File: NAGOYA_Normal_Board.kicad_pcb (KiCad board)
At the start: 2 copper layers, 60 x 71 mm, 104 parts, among them CN1 XT30-M, CN13 value, CN14 RefereeSystem, CN15 micro_B, CN2 XT30-M, CN3 XT30-F, CN4 XT30-F, CN5 XT30-F, CN6 XT30-F, J1 debug, J10 CAN3, J13 CAN3, J14 CAN3, J5 CAN3, J6 CAN3, J7 CAN3, J8 CAN3, J9 CAN3, Q2 DDTC114EUA-7-F, Q4 DDTC114EUA-7-F, Q5 DDTC114EUA-7-F, Q6 DDTC114EUA-7-F, SW1 SW_DIP_x04, U1 Teensy4.1, U2 TCAN1042HVDR, U3 TCAN1042HVDR, U4 TCAN1042HVDR, U5 FT234XD, U6 TLP172AM, U7 BNO055, U8 ADuM121N, U9 LXES11DAA2-137, Y2 32.768 k

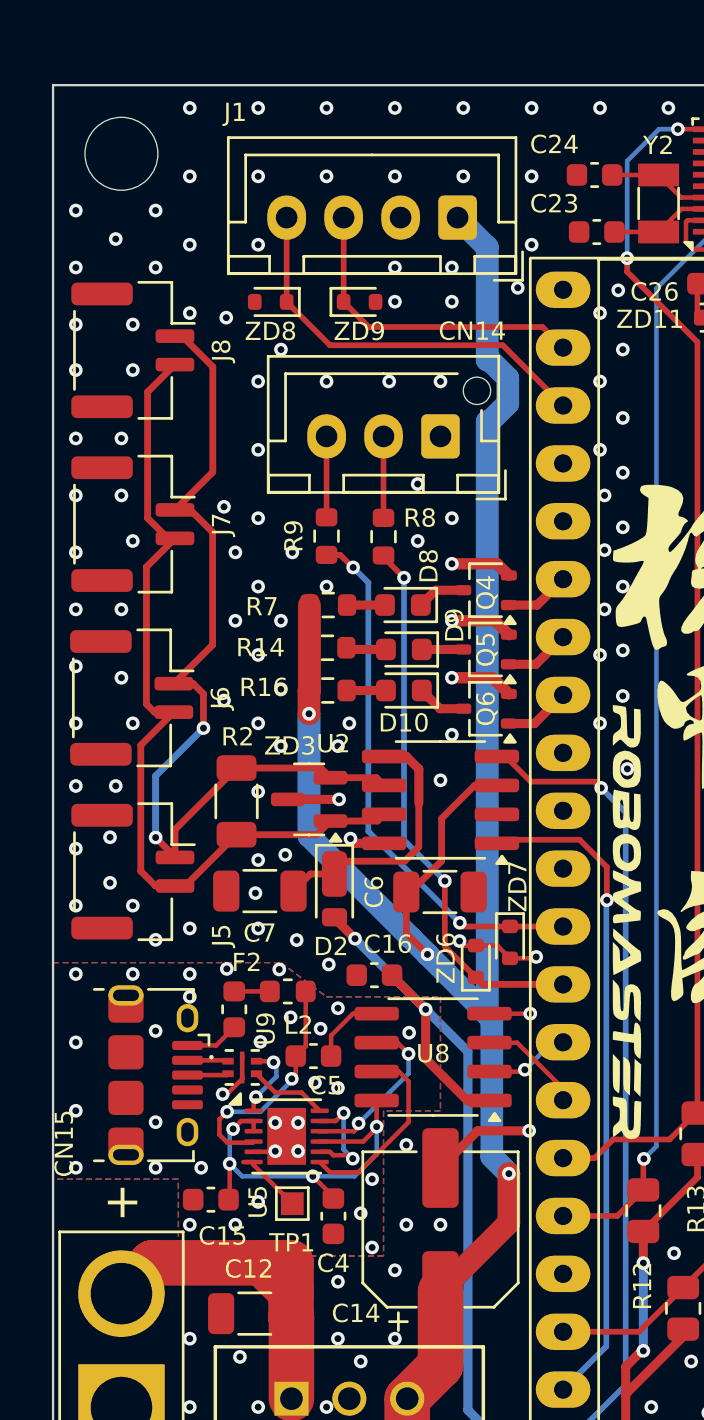
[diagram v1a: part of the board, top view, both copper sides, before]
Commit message: USBを削除パターンを変更
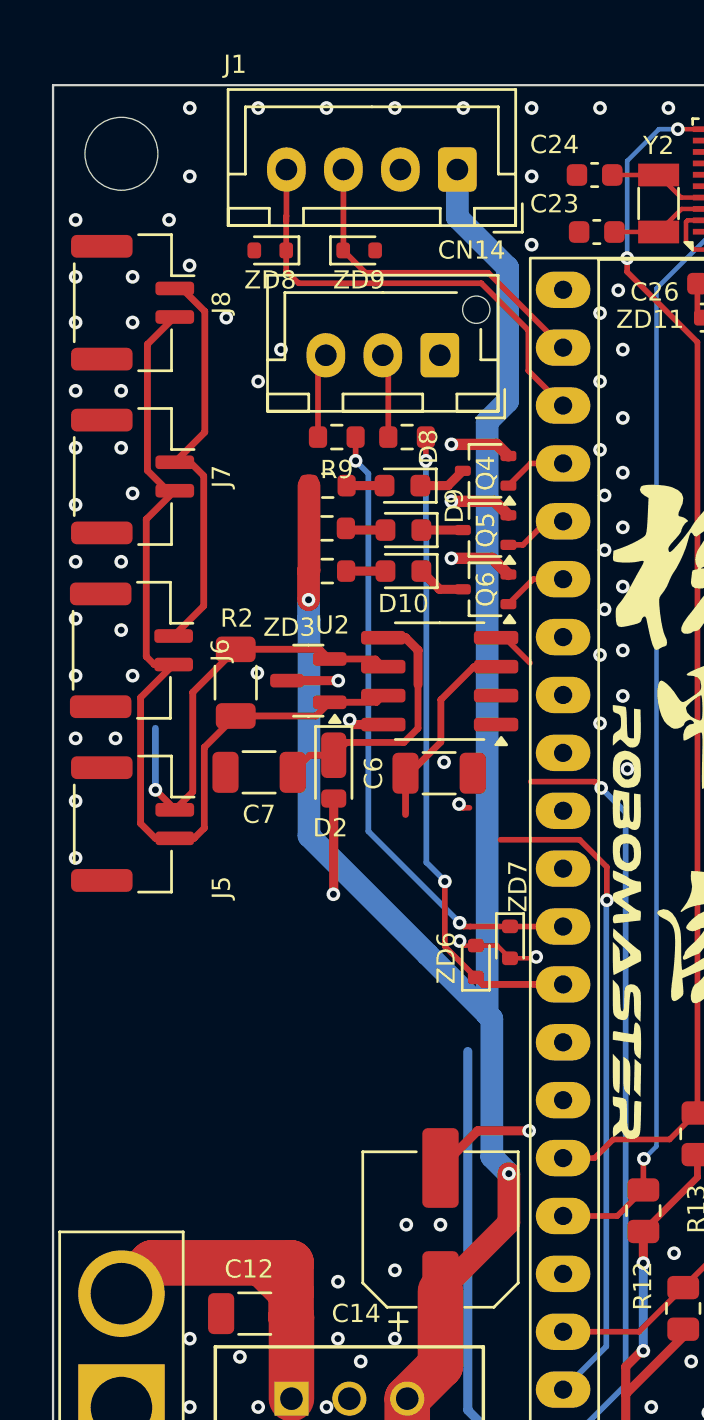
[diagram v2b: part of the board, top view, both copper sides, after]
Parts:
- removed C15, C16, C4, C5: 0.1u, Capacitor_SMD:C_0603_1608Metric
- removed CN15: micro_B, Connector_USB:USB_Micro-B_Amphenol_10118194-0001LF_Horizontal
- removed F2: Fuse_Small, Fuse:Fuse_0603_1608Metric
- removed L2: L, Inductor_SMD:L_0603_1608Metric
- removed TP1: TestPoint, TestPoint:TestPoint_Pad_1.0x1.0mm
- removed U5: FT234XD, Package_DFN_QFN:WDFN-12-1EP_3x3mm_P0.45mm_EP1.7x2.5mm
- removed U8: ADuM121N, Package_SO:SOIC-8_3.9x4.9mm_P1.27mm
- removed U9: LXES11DAA2-137, 0_PCB:FIL_LXES11DAA2-137
- moved Q4 5.24 mm to (129.0, 70.9)
- moved D10 5.24 mm to (125.4, 75.3)
- moved D8 5.24 mm to (125.3, 71.6)
- moved D9 5.24 mm to (125.4, 73.5)
- moved Q5 5.24 mm to (129.0, 73.5)
- moved Q6 5.24 mm to (129.0, 76.1)
- moved R14 5.24 mm to (122.0, 73.4)
- moved R16 5.24 mm to (122.0, 75.3)
- moved R7 5.24 mm to (122.1, 71.6)
- moved R2 5.21 mm to (118.0, 80.2)
- moved C6 5.21 mm to (126.9, 84.2)
- moved C7 5.21 mm to (119.0, 84.1)
- moved D2 5.21 mm to (122.3, 84.0)
- moved U2 5.21 mm to (127.0, 80.1)
- moved ZD3 5.21 mm to (121.2, 80.1)
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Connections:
- U1 pad 28: unconnected-(U1-36-Pad28) -> LED2
- U1 pad 29: unconnected-(U1-37-Pad29) -> LED3
- U1 pad 30: LED2 -> LED4
- U1 pad 31: LED3 -> unconnected-(U1-39-Pad31)
- U1 pad 32: LED4 -> unconnected-(U1-40-Pad32)
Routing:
- net Net-(U5-3V3OUT): track 18.3 -> 0.00 mm, vias 4 -> 0
- net +3.3V: track 206.1 -> 194.2 mm, vias 10 -> 9
- net Net-(U5-VCC): track 10.4 -> 0.00 mm, vias 2 -> 0
- net Net-(U5-TXD/D0): track 8.37 -> 0.00 mm
- net Net-(U5-RXD/D1): track 7.50 -> 0.00 mm, vias 2 -> 0
- net GNDREF: track 7.16 -> 0.00 mm, vias 31 -> 0
- net +5V: track 159.3 -> 165.2 mm, vias 3 -> 2
- net TX3: track 23.5 -> 28.5 mm, vias 2 -> 3
- net Net-(U5-~{CTS}/D3): track 4.95 -> 0.00 mm, vias 2 -> 0
- net RX3: track 24.1 -> 28.9 mm, vias 2 -> 3
- net UART4_TX: track 4.77 -> 0.71 mm
- net Net-(U5-USBDP): track 3.45 -> 0.00 mm
- net CAN1_L: track 40.3 -> 36.9 mm, vias 2 -> 1
- net UART4_RX: track 5.00 -> 1.63 mm, vias 1 -> 0
- net Net-(U5-USBDM): track 3.36 -> 0.00 mm, vias 2 -> 0
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- removed copper zone on B.Cu, net GNDREF
- removed copper zone on F.Cu, net GNDREF
